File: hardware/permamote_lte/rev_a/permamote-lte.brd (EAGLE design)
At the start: 27 x 60 mm, 116 parts, among them J1 TC2030-JLINK-NL, J2 U.FL-R-SMT, J3 NANO_SIM, J4 U.FL-R-SMT, J5 DM3AT-SF-PEJM5, Q1 PMDXB950UPEL, Q10 PMDXB950UPEL, Q2 PMDXB950UPEL, Q3 PMDXB950UPEL, Q4 PMDXB950UPEL, Q5 PMDXB950UPEL, Q6 PMDXB950UPEL, Q7 PMDXB950UPEL, Q8 PMDXB950UPEL, U1 AB1815-T3, U10 SIP32510, U11 SI7021-A20-GM1, U12 TCS34725, U13 TPD3F303DPVR, U2 BQ25505, U3 EKMB1101111, U4 BGA725L6, U5 NRF9160, U6 LIS2DW12, U7 MAX17222, U8 MAX44009, U9 MS5637-02BA03, X4 ABS07-32.768KHZ-7-T

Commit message: fixes
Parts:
- moved C17 0.77 mm to (21.2, 44.8)
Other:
- board text added: "Permamote_LTE Meghna Mandava 5/20"
- board text removed: "Permamote_LTE Meghna Mandava 4/20"
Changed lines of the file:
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@@
 <?xml version="1.0" encoding="utf-8"?>
 <!DOCTYPE eagle SYSTEM "eagle.dtd">
-<eagle version="9.5.0">
+<eagle version="9.6.1">
 <drawing>
 <settings>
@@
 <text x="0.794" y="27.697" size="1.016" layer="25" font="vector" ratio="12" align="top-left">Permamote_LTE
 Meghna Mandava
-4/20</text>
+5/20</text>
 <polygon width="0.1016" layer="41">
 <vertex x="24.3713" y="17.018"/>
@@
 <wire x1="11.43" y1="37.63" x2="12.6" y2="37.63" width="0.1524" layer="25"/>
 <wire x1="12.6" y1="37.63" x2="12.6" y2="36.106" width="0.1524" layer="25"/>
-<text x="26.416" y="32.639" size="0.8128" layer="25" font="vector" ratio="12" align="center-right">GND</text>
+<text x="26.416" y="32.512" size="0.8128" layer="25" font="vector" ratio="12" align="center-right">GND</text>
 <text x="26.162" y="31.242" size="0.8128" layer="25" font="vector" ratio="12" align="center-right">VCC</text>
 <wire x1="0" y1="60" x2="0.5" y2="60" width="0" layer="20"/>
@@
 <param name="tpViaShape" value="round"/>
 <param name="PrefDir.1" value="-"/>
-<param name="PrefDir.2" value="*"/>
+<param name="PrefDir.2" value="0"/>
 <param name="PrefDir.3" value="0"/>
 <param name="PrefDir.4" value="0"/>
@@
 <param name="PrefDir.13" value="0"/>
 <param name="PrefDir.14" value="0"/>
-<param name="PrefDir.15" value="*"/>
+<param name="PrefDir.15" value="0"/>
 <param name="PrefDir.16" value="|"/>
 <param name="cfVia" value="8"/>
@@
 <attribute name="NAME" x="22.336" y="43.675" size="0.8128" layer="25" font="vector" ratio="12" align="bottom-center"/>
 </element>
-<element name="C17" library="passives" package="0603_CAP" value="10uF" x="21.082" y="45.593" smashed="yes" rot="R180">
-<attribute name="DIGIKEY" value="490-3896-1-ND" x="21.082" y="45.593" size="1.778" layer="27" rot="R180" display="off"/>
-<attribute name="MPN" value="GRM188R60J106ME47D " x="21.082" y="45.593" size="1.778" layer="27" rot="R180" display="off"/>
-<attribute name="NAME" x="19.05" y="45.212" size="0.8128" layer="25" font="vector" ratio="12" align="bottom-center"/>
+<element name="C17" library="passives" package="0603_CAP" value="10uF" x="21.209" y="44.831" smashed="yes" rot="R180">
+<attribute name="DIGIKEY" value="490-3896-1-ND" x="21.209" y="44.831" size="1.778" layer="27" rot="R180" display="off"/>
+<attribute name="MPN" value="GRM188R60J106ME47D " x="21.209" y="44.831" size="1.778" layer="27" rot="R180" display="off"/>
+<attribute name="NAME" x="19.177" y="44.577" size="0.8128" layer="25" font="vector" ratio="12" align="bottom-center"/>
 </element>
 <element name="C18" library="passives" package="0603_CAP" value="10uF" x="18.923" y="40.767" smashed="yes" rot="R180">
@@
 <attribute name="DIGIKEY" value="541-100MAHCT-ND" x="22.352" y="22.352" size="1.778" layer="27" display="off"/>
 <attribute name="MPN" value="HMC0402JT100M " x="22.352" y="22.352" size="1.778" layer="27" display="off"/>
-<attribute name="NAME" x="22.225" y="23.622" size="0.8128" layer="25" font="vector" ratio="12" rot="R180" align="bottom-center"/>
+<attribute name="NAME" x="21.971" y="23.495" size="0.8128" layer="25" font="vector" ratio="12" rot="R180" align="bottom-center"/>
 <attribute name="VALUE" x="22.352" y="20.955" size="1.016" layer="27" font="vector" ratio="12" align="bottom-center"/>
 </element>
@@
 <attribute name="MANUFACTURER" value="NEXPERIA" x="5.334" y="13.843" size="1.778" layer="27" rot="R90" display="off"/>
 <attribute name="MPN" value="PMDXB950UPELZ" x="5.334" y="13.843" size="1.778" layer="27" rot="R90" display="off"/>
-<attribute name="NAME" x="5.334" y="12.954" size="0.8128" layer="25" font="vector" ratio="12" rot="R180" align="bottom-center"/>
+<attribute name="NAME" x="5.334" y="12.446" size="0.8128" layer="25" font="vector" ratio="12" rot="R180" align="bottom-center"/>
 <attribute name="VALUE" x="6.334" y="13.843" size="1.016" layer="27" font="vector" ratio="12" rot="R90" align="top-center"/>
 </element>
@@
 <attribute name="MANUFACTURER" value="NEXPERIA" x="21.082" y="1.905" size="1.778" layer="27" display="off"/>
 <attribute name="MPN" value="PMDXB950UPELZ" x="21.082" y="1.905" size="1.778" layer="27" display="off"/>
-<attribute name="NAME" x="20.955" y="1.159" size="0.8128" layer="25" font="vector" ratio="12" rot="R180" align="bottom-center"/>
+<attribute name="NAME" x="21.082" y="1.032" size="0.8128" layer="25" font="vector" ratio="12" rot="R180" align="bottom-center"/>
 <attribute name="VALUE" x="21.082" y="0.905" size="1.016" layer="27" font="vector" ratio="12" align="top-center"/>
 </element>
@@
 <attribute name="MANUFACTURER" value="NEXPERIA" x="5.334" y="16.383" size="1.778" layer="27" display="off"/>
 <attribute name="MPN" value="PMDXB950UPELZ" x="5.334" y="16.383" size="1.778" layer="27" display="off"/>
-<attribute name="NAME" x="5.334" y="17.272" size="0.8128" layer="25" font="vector" ratio="12" align="bottom-center"/>
+<attribute name="NAME" x="5.334" y="17.526" size="0.8128" layer="25" font="vector" ratio="12" align="bottom-center"/>
 <attribute name="VALUE" x="5.334" y="15.383" size="1.016" layer="27" font="vector" ratio="12" align="top-center"/>
 </element>
@@
 </element>
 <element name="L3" library="passives" package="0402_CAP" value="7.5nH" x="5.842" y="50.927" smashed="yes" rot="R90">
+<attribute name="DIGIKEY" value="490-6565-1-ND" x="5.842" y="50.927" size="1.778" layer="27" rot="R90" display="off"/>
+<attribute name="MPN" value="LQG15HN7N5J02D" x="5.842" y="50.927" size="1.778" layer="27" rot="R90" display="off"/>
 <attribute name="NAME" x="5.461" y="50.927" size="0.8128" layer="25" font="vector" ratio="12" rot="R90" align="bottom-center"/>
 </element>
@@
 </element>
 <element name="L2" library="passives" package="0402_CAP" value="5.1nH" x="5.842" y="52.578" smashed="yes" rot="R90">
+<attribute name="DIGIKEY" value="490-6564-1-ND" x="5.842" y="52.578" size="1.778" layer="27" rot="R90" display="off"/>
+<attribute name="MPN" value="LQG15HN5N1S02D" x="5.842" y="52.578" size="1.778" layer="27" rot="R90" display="off"/>
 <attribute name="NAME" x="6.985" y="52.959" size="0.8128" layer="25" font="vector" ratio="12" rot="R90" align="bottom-center"/>
 </element>
 <element name="L1" library="passives" package="0402_CAP" value="1.8nH" x="7.62" y="51.308" smashed="yes" rot="R180">
+<attribute name="DIGIKEY" value="490-2613-1-ND" x="7.62" y="51.308" size="1.778" layer="27" rot="R180" display="off"/>
+<attribute name="MPN" value="LQG15HS1N8S02D" x="7.62" y="51.308" size="1.778" layer="27" rot="R180" display="off"/>
 <attribute name="NAME" x="7.62" y="52.578" size="0.8128" layer="25" font="vector" ratio="12" rot="R180" align="bottom-center"/>
 </element>
@@
 <attribute name="MANUFACTURER" value="Samsung Electro-Mechanics" x="45.72" y="63.754" size="1.778" layer="27" rot="R270" display="off"/>
 <attribute name="MPN" value="RC1005F103CS" x="45.72" y="63.754" size="1.778" layer="27" rot="R270" display="off"/>
-<attribute name="NAME" x="24.13" y="38.989" size="0.8128" layer="25" font="vector" ratio="12" rot="R270" align="bottom-center"/>
+<attribute name="NAME" x="24.13" y="39.243" size="0.8128" layer="25" font="vector" ratio="12" rot="R270" align="bottom-center"/>
 <attribute name="VALUE" x="22.352" y="38.989" size="1.016" layer="27" font="vector" ratio="12" rot="R270" align="bottom-center"/>
 </element>
@@
 <attribute name="MANUFACTURER" value="Vishay Dale" x="5.715" y="44.704" size="1.778" layer="27" display="off"/>
 <attribute name="MPN" value="CRCW0402100KFKEDHP" x="5.715" y="44.704" size="1.778" layer="27" display="off"/>
-<attribute name="NAME" x="23.749" y="33.02" size="0.8128" layer="25" font="vector" ratio="12" align="bottom-center"/>
+<attribute name="NAME" x="23.876" y="33.02" size="0.8128" layer="25" font="vector" ratio="12" align="bottom-center"/>
 <attribute name="VALUE" x="23.749" y="32.766" size="1.016" layer="27" font="vector" ratio="12" align="bottom-center"/>
 </element>
@@
 <polygon width="0.2032" layer="1" isolate="0.2032" thermals="no">
 <vertex x="21.59" y="42.799"/>
-<vertex x="21.59" y="44.958"/>
-<vertex x="21.209" y="44.958"/>
-<vertex x="21.209" y="46.101"/>
+<vertex x="21.59" y="46.101"/>
 <vertex x="25.527" y="46.101"/>
 <vertex x="25.527" y="43.815"/>
@@
 <wire x1="18.891" y1="44.958" x2="22.86" y2="44.958" width="0.254" layer="16"/>
 <via x="22.86" y="44.958" extent="1-16" drill="0.2032"/>
-<wire x1="21.732" y1="45.593" x2="20.97" y2="44.831" width="0.1524" layer="1"/>
-<wire x1="20.97" y1="44.831" x2="19.035" y2="44.831" width="0.1524" layer="1"/>
-<wire x1="18.273" y1="44.069" x2="19.035" y2="44.831" width="0.1524" layer="1"/>
+<wire x1="21.859" y1="44.831" x2="21.097" y2="45.593" width="0.1524" layer="1"/>
+<wire x1="21.097" y1="45.593" x2="19.797" y2="45.593" width="0.1524" layer="1"/>
+<wire x1="18.273" y1="44.069" x2="19.797" y2="45.593" width="0.1524" layer="1"/>
 </signal>
 <signal name="VBAT">
@@
 <wire x1="14.859" y1="34.036" x2="13.502" y2="34.036" width="0.1524" layer="1"/>
 <wire x1="13.466" y1="34" x2="13.502" y2="34.036" width="0.1524" layer="1"/>
-<via x="12.319" y="13.335" extent="1-16" drill="0.2032"/>
+<via x="12.319" y="13.208" extent="1-16" drill="0.2032"/>
 <via x="18.796" y="36.068" extent="1-16" drill="0.2032"/>
 <wire x1="18.796" y1="36.068" x2="18.796" y2="32.35418125" width="0.4064" layer="1"/>
@@
 <wire x1="14.097" y1="28.575" x2="14.097" y2="22.225" width="0.4064" layer="1"/>
 <wire x1="14.097" y1="22.225" x2="12.319" y2="20.447" width="0.4064" layer="1"/>
-<wire x1="12.319" y1="20.447" x2="12.319" y2="13.335" width="0.4064" layer="1"/>
+<wire x1="12.319" y1="20.447" x2="12.319" y2="13.208" width="0.4064" layer="1"/>
 <wire x1="12.319" y1="4.953" x2="14.097" y2="3.175" width="0.4064" layer="16"/>
-<wire x1="12.319" y1="13.335" x2="12.319" y2="4.953" width="0.4064" layer="16"/>
+<wire x1="12.319" y1="13.208" x2="12.319" y2="4.953" width="0.4064" layer="16"/>
 <wire x1="18.796" y1="32.35418125" x2="18.44581875" y2="32.004" width="0.4064" layer="1"/>
 <wire x1="18.44581875" y1="32.004" x2="18.415" y2="32.004" width="0.4064" layer="1"/>

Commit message: outline, label fixes
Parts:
- moved TP9 3.35 mm to (19.3, 2.16)
- moved R21 0.52 mm to (18.4, 44.2), turned to 90 degrees
- moved U8 0.51 mm to (17.5, 2.54)
- moved Q3 0.38 mm to (17.4, 5.33)
- moved TP1 0.25 mm to (26.0, 5.08)
- moved Q7 0.25 mm to (21.1, 2.16)
- moved C17 0.13 mm to (21.2, 44.7)
- moved R14 0.13 mm to (18.9, 42.3)
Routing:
- net N$14: track 1.85 -> 2.79 mm
- net SDA: track 58.7 -> 57.8 mm
- net !CLR_EN: track 50.5 -> 49.7 mm
- net !LT_INT: track 45.2 -> 44.7 mm
- net GND: track 31.5 -> 31.1 mm, vias 97 -> 99
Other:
- outline, holes or cut-outs redrawn

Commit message: renumber
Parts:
- removed TP30: TEST-POINT, headers:PAD.03X.03
- added TP24: TEST-POINT, headers:PAD.03X.03
- J1: value TC2030-JLINK-NL -> DM3AT-SF-PEJM5; device connector:TC2030-IDC-NL -> connector:DM3AT-SF-PEJM5
- J2: value U.FL-R-SMT -> NANO_SIM; device connector:U.FL_SMT -> signpost:WURTH_NANO_SIM
- J3: value NANO_SIM -> TC2030-JLINK-NL; device signpost:WURTH_NANO_SIM -> connector:TC2030-IDC-NL
- J5: value DM3AT-SF-PEJM5 -> U.FL-R-SMT; device connector:DM3AT-SF-PEJM5 -> connector:U.FL_SMT
- U10: value SIP32510 -> SI7021-A20-GM1; device chips:TSOT23-6 -> chips:DFN-6/3MM
- U11: value SI7021-A20-GM1 -> SIP32510; device chips:DFN-6/3MM -> chips:TSOT23-6
- U2: value BQ25505 -> BGA725L6; device chips:S-PVQFN-N20-RGR -> chips:LNA-TSLP-6-2-ORIG
- U3: value EKMB1101111 -> BQ25505; device chips:AMN2 -> chips:S-PVQFN-N20-RGR
- U4: value BGA725L6 -> EKMB1101111; device chips:LNA-TSLP-6-2-ORIG -> chips:AMN2
- U5: value NRF9160 -> LIS2DW12; device chips:NRF9160 -> chips:LGA-12
- U6: value LIS2DW12 -> MAX17222; device chips:LGA-12 -> chips:UDFN-6-MAXIM
- U7: value MAX17222 -> MAX44009; device chips:UDFN-6-MAXIM -> chips:UDFN-6-EXPOSED
- U8: value MAX44009 -> MS5637-02BA03; device chips:UDFN-6-EXPOSED -> chips:4-SMD
- U9: value MS5637-02BA03 -> NRF9160; device chips:4-SMD -> chips:NRF9160
- moved U3 49.6 mm to (19.9, 53.1), turned to 90 degrees
- moved U4 43.8 mm to (5.50, 5.56), turned to 0 degrees
- moved U7 40.0 mm to (17.5, 2.54)
- moved U10 27.7 mm to (2.02, 19.9)
- moved U11 27.7 mm to (24.1, 36.6)
- moved U6 24.9 mm to (21.7, 42.3), turned to 90 degrees
- moved J2 23.0 mm to (6.99, 35.2), flipped to the bottom, turned to 90 degrees
- moved U9 21.8 mm to (13.7, 31.8)
- moved J3 19.8 mm to (24.5, 26.0), flipped to the top
- moved U8 18.9 mm to (2.03, 13.3)
- moved J5 18.4 mm to (2.29, 51.2), flipped to the top, turned to 90 degrees
- moved J1 18.3 mm to (18.9, 43.4), flipped to the bottom, turned to 180 degrees
- moved U5 17.8 mm to (24.4, 17.5), turned to 0 degrees
- moved U2 14.8 mm to (5.59, 49.4)
- moved TP25 10.3 mm to (25.4, 30.5)
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- renumbered BAT1 to BT2, Q10 to Q9, TP31 to TP28, TP32 to TP29, X4 to X1
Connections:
- net !CLR_EN: now also U9.P0.08; no longer U5.P0.08
- net !CLR_INT: now also U9.P0.29; no longer U5.P0.29
- net !HUM_EN: now also U9.P0.04; no longer U5.P0.04
- net !LT_EN: now also U9.P0.30; no longer U5.P0.30
- net !LT_INT: now also U7.4, U9.P0.02; no longer U5.P0.02, U8.4
- net !PIR_EN: now also U9.P0.24; no longer U5.P0.24
- net !PR_EN: now also U9.P0.23; no longer U5.P0.23
- net !RST: now also J3.3, U9.NRESET; no longer J1.3, U5.NRESET
- net !RTC_IRQ1: now also U9.P0.11; no longer U5.P0.11
- net !RTC_IRQ2: now also U9.P0.10; no longer U5.P0.10
- net !RTC_IRQ3: now also U9.P0.09; no longer U5.P0.09
- net !SD_CS: now also J1.2, U9.P0.26; no longer J5.2, U5.P0.26
- net !SD_DETECT: now also J1.A, U9.P0.27; no longer J5.A, U5.P0.27
- net !VBAT_PRI_ON: now also U3.10; no longer U2.10
- net !VBAT_SEC_ON: now also U3.9; no longer U2.9
- net ACC_CS: now also U5.2, U9.P0.06; no longer U5.P0.06, U6.2
- net ACC_INT1: now also U5.12, U9.P0.05; no longer U5.P0.05, U6.12
- net ACC_INT2: now also U5.11, U9.P0.07; no longer U5.P0.07, U6.11
- net GND: now also J1.6, J1.B, J1.MOUNT0, J1.MOUNT1, J1.MOUNT2, J1.MOUNT3, J2.C5, J3.5, J5.GND1, J5.GND2, TP26.P$1, U10.2, U11.4, U2.4, U3.1, U3.15, U3.16, U3.17, U3.5, U3.6, U3.PAD, U4.GND, U5.5, U5.6, U5.7, U5.8, U6.3, U7.2, U7.EP, U8.4, U9.GND@1, U9.GND@10, U9.GND@11, U9.GND@12, U9.GND@13, U9.GND@14, U9.GND@15, U9.GND@16, U9.GND@17, U9.GND@18, U9.GND@19, U9.GND@2, U9.GND@20, U9.GND@21, U9.GND@22, U9.GND@23, U9.GND@24, U9.GND@25, U9.GND@26, U9.GND@27, U9.GND@28, U9.GND@29, U9.GND@3, U9.GND@30, U9.GND@31, U9.GND@32, U9.GND@33, U9.GND@34, U9.GND@35, U9.GND@4, U9.GND@5, U9.GND@6, U9.GND@7, U9.GND@8, U9.GND@9, U9.GND_SHIELD@1, U9.GND_SHIELD@10, U9.GND_SHIELD@11, U9.GND_SHIELD@12, U9.GND_SHIELD@13, U9.GND_SHIELD@14, U9.GND_SHIELD@15, U9.GND_SHIELD@16, U9.GND_SHIELD@17, U9.GND_SHIELD@18, U9.GND_SHIELD@19, U9.GND_SHIELD@2, U9.GND_SHIELD@20, U9.GND_SHIELD@21, U9.GND_SHIELD@22, U9.GND_SHIELD@23, U9.GND_SHIELD@24, U9.GND_SHIELD@25, U9.GND_SHIELD@26, U9.GND_SHIELD@27, U9.GND_SHIELD@28, U9.GND_SHIELD@29, U9.GND_SHIELD@3, U9.GND_SHIELD@30, U9.GND_SHIELD@31, U9.GND_SHIELD@32, U9.GND_SHIELD@33, U9.GND_SHIELD@34, U9.GND_SHIELD@4, U9.GND_SHIELD@5, U9.GND_SHIELD@6, U9.GND_SHIELD@7, U9.GND_SHIELD@8, U9.GND_SHIELD@9; no longer J1.5, J2.GND1, J2.GND2, J3.C5, J5.6, J5.B, J5.MOUNT0, J5.MOUNT1, J5.MOUNT2, J5.MOUNT3, TP27.P$1, U10.4, U11.2, U2.15, U2.16, U2.17, U2.5, U2.6, U2.PAD, U3.GND, U4.1, U4.4, U5.GND@1, U5.GND@10, U5.GND@11, U5.GND@12, U5.GND@13, U5.GND@14, U5.GND@15, U5.GND@16, U5.GND@17, U5.GND@18, U5.GND@19, U5.GND@2, U5.GND@20, U5.GND@21, U5.GND@22, U5.GND@23, U5.GND@24, U5.GND@25, U5.GND@26, U5.GND@27, U5.GND@28, U5.GND@29, U5.GND@3, U5.GND@30, U5.GND@31, U5.GND@32, U5.GND@33, U5.GND@34, U5.GND@35, U5.GND@4, U5.GND@5, U5.GND@6, U5.GND@7, U5.GND@8, U5.GND@9, U5.GND_SHIELD@1, U5.GND_SHIELD@10, U5.GND_SHIELD@11, U5.GND_SHIELD@12, U5.GND_SHIELD@13, U5.GND_SHIELD@14, U5.GND_SHIELD@15, U5.GND_SHIELD@16, U5.GND_SHIELD@17, U5.GND_SHIELD@18, U5.GND_SHIELD@19, U5.GND_SHIELD@2, U5.GND_SHIELD@20, U5.GND_SHIELD@21, U5.GND_SHIELD@22, U5.GND_SHIELD@23, U5.GND_SHIELD@24, U5.GND_SHIELD@25, U5.GND_SHIELD@26, U5.GND_SHIELD@27, U5.GND_SHIELD@28, U5.GND_SHIELD@29, U5.GND_SHIELD@3, U5.GND_SHIELD@30, U5.GND_SHIELD@31, U5.GND_SHIELD@32, U5.GND_SHIELD@33, U5.GND_SHIELD@34, U5.GND_SHIELD@4, U5.GND_SHIELD@5, U5.GND_SHIELD@6, U5.GND_SHIELD@7, U5.GND_SHIELD@8, U5.GND_SHIELD@9, U6.5, U6.6, U6.7, U6.8, U8.2, U8.3, U8.EP, U9.4
- net GPS_EN: now also U2.6, U9.MAGPIO0; no longer U4.6, U5.MAGPIO0
- net LBST: now also U3.20; no longer U2.20
- net LED_BLUE: now also U9.P0.17; no longer U5.P0.17
- net LED_GREEN: now also U9.P0.19; no longer U5.P0.19
- net LED_RED: now also U9.P0.18; no longer U5.P0.18
- net MISO: now also J1.7, U5.3, U9.P0.22; no longer J5.7, U5.P0.22, U6.3
- net MOSI: now also J1.3, U5.4, U9.P0.21; no longer J5.3, U5.P0.21, U6.4
- net N$1: now also U2.3, U9.GPS; no longer U4.3, U5.GPS
- net N$12: now also U6.4; no longer U7.4
- net N$13: now also J1.4, U11.1, U11.2; no longer J5.4, U10.1, U10.2
- net N$14: now also U6.6; no longer U7.6
- net N$18: now also U3.7; no longer U2.7
- net N$2: now also U2.5; no longer U4.5
- net N$20: now also U7.1; no longer U8.1
- net N$21: now also U8.1; no longer U9.1
- net N$22: now also U10.5; no longer U11.5
- net N$23: now also U4.VCC; no longer U3.VCC
- net N$28: now also U9.ENABLE; no longer U5.ENABLE
- net N$29: now also U9.IO_SUPPLY; no longer U5.IO_SUPPLY
- net N$32: now also U3.8; no longer U2.8
- net N$34: now also U8.3; no longer U9.3
- net N$4: now also J5.SIG; no longer J4.SIG
- net N$41: now also U8.2; no longer U9.2
- net N$48: now also U10.1; no longer U11.1
- net N$50: now also U10.6; no longer U11.6
- net N$51: now also U7.6; no longer U8.6
- net N$52: now also U7.5; no longer U8.5
- net N$57: now also U3.12; no longer U2.12
- net N$58: now also U3.11; no longer U2.11
- net N$8: now also J4.SIG, U9.ANT; no longer J2.SIG, U5.ANT
- net PIR_OUT: now also U4.OUT, U9.P0.25; no longer U3.OUT, U5.P0.25
- net RTC_CS: now also U9.P0.12; no longer U5.P0.12
- net SCK: now also J1.5, U5.1, U9.P0.03; no longer J5.5, U5.P0.03, U6.1
- net SCL: now also U9.P0.01; no longer U5.P0.01
- net SDA: now also U9.P0.00; no longer U5.P0.00
- net SD_ENABLE: now also U11.3, U9.P0.28; no longer U10.3, U5.P0.28
- net SIM_1V8: now also J2.C1, U9.SIM_1V8; no longer J3.C1, U5.SIM_1V8
- net SIM_CLK: now also U9.SIM_CLK; no longer U5.SIM_CLK
- net SIM_CLK2: now also J2.C3; no longer J3.C3
- net SIM_IO: now also U9.SIM_IO; no longer U5.SIM_IO
- net SIM_IO2: now also J2.C7; no longer J3.C7
- net SIM_RST: now also U9.SIM_RST; no longer U5.SIM_RST
- net SIM_RST2: now also J2.C2, TP27.P$1; no longer J3.C2, TP30.P$1
- net SW: now also TP24.P$1, U6.2; no longer TP25.P$1, U7.2
- net SWDCLK: now also J3.4, U9.SWDCLK; no longer J1.4, U5.SWDCLK
- net SWDIO: now also J3.2, U9.SWDIO; no longer J1.2, U5.SWDIO
- net VBAT: now also U3.14, U9.P0.15; no longer U2.14, U5.P0.15
- net VBAT_OK: now also U3.13, U9.P0.20; no longer U2.13, U5.P0.20
- net VCC: now also J3.1, TP25.P$1, U11.5, U11.6, U2.2, U5.10, U5.9, U6.1, U9.VDD@1, U9.VDD@2, U9.VDD_GPIO; no longer J1.1, TP26.P$1, U10.5, U10.6, U4.2, U5.VDD@1, U5.VDD@2, U5.VDD_GPIO, U6.10, U6.9, U7.1
- net VOC_SAMP_VSTOR: now also U3.19, U3.3; no longer U2.19, U2.3
- net VREF_SAMP: now also U3.4; no longer U2.4
- net VSEC: now also U3.18, U9.P0.13; no longer U2.18, U5.P0.13
- net VSOL: now also U3.2, U9.P0.14; no longer U2.2, U5.P0.14
- net VSW: now also U6.5; no longer U7.5
- net WDI: now also U9.P0.16; no longer U5.P0.16

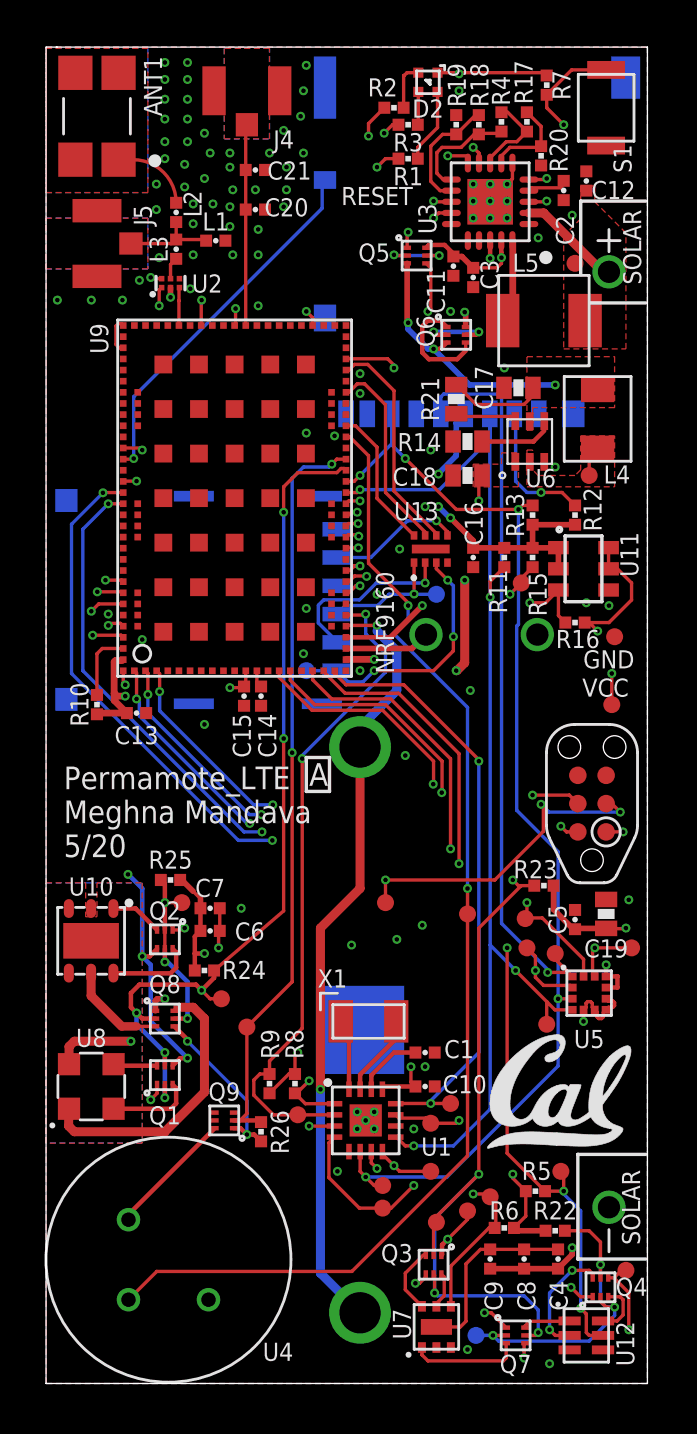
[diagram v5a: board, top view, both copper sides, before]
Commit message: pins overlapping cage need to fix
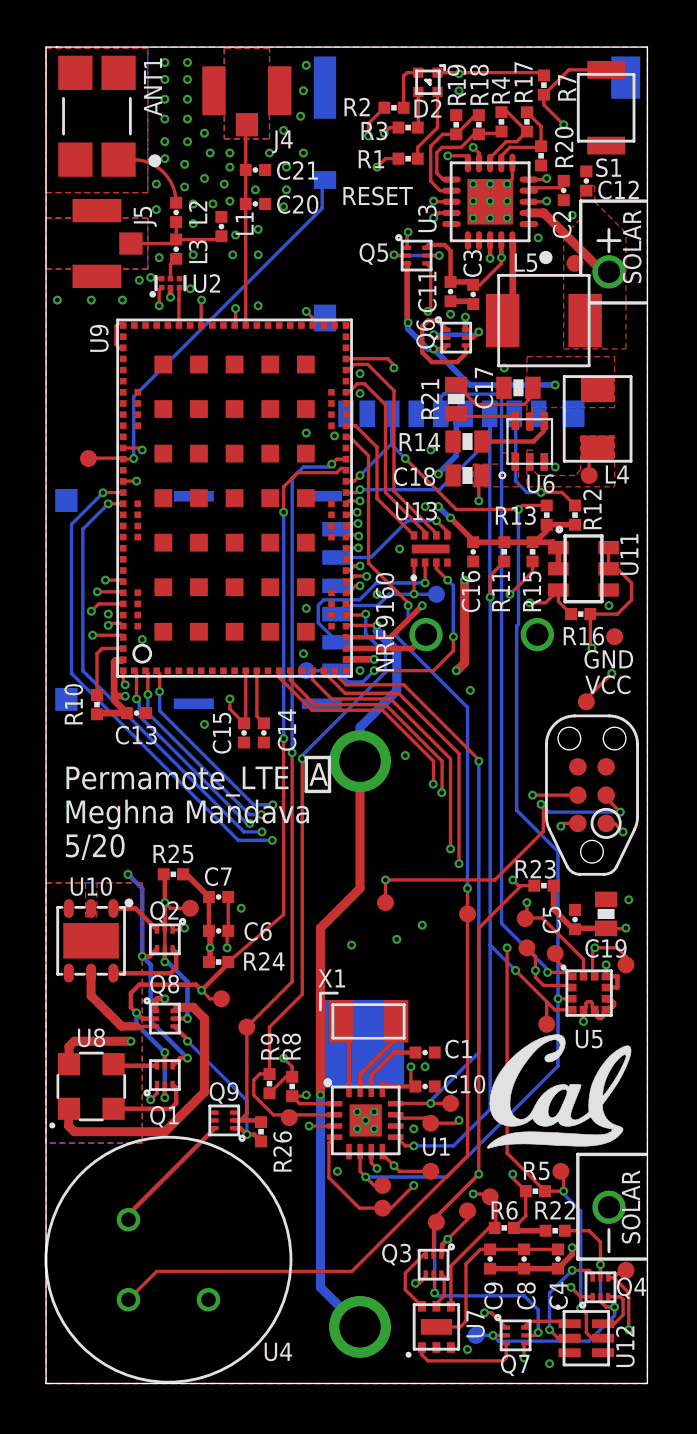
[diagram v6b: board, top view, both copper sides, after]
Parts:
- moved TP29 20.2 mm to (1.91, 41.5)
- moved C14 1.66 mm to (9.78, 29.2)
- moved C15 1.65 mm to (8.89, 29.2)
- moved C11 1.15 mm to (18.2, 49.0)
- moved TP25 1.15 mm to (24.3, 30.6)
- moved TP19 0.80 mm to (26.0, 18.8)
- moved C3 0.76 mm to (19.2, 48.9)
- moved R24 0.74 mm to (7.75, 18.9)
- moved L1 0.68 mm to (7.87, 51.9), turned to 270 degrees
- moved C7 0.64 mm to (7.75, 21.8)
- moved BT2 0.63 mm to (14.1, 15.2)
- moved R13 0.63 mm to (22.5, 39.0)
- moved R16 0.46 mm to (24.0, 34.5)
- moved TP12 0.46 mm to (6.48, 21.3)
- moved TP16 0.40 mm to (10.9, 11.9)
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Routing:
- net VCC: track 62.9 -> 65.4 mm
- net !SD_DETECT: track 40.2 -> 42.1 mm
- net GND: track 31.1 -> 32.8 mm, vias 99 -> 98
- net N$29: track 0.78 -> 2.49 mm
- net VOC_SAMP_VSTOR: track 9.24 -> 10.6 mm
- net !RST: track 45.0 -> 45.8 mm
- net VBAT: track 63.2 -> 64.0 mm
- net N$4: track 4.29 -> 4.98 mm
- net !HUM_EN: track 23.6 -> 24.2 mm
- net MISO: track 52.4 -> 53.1 mm
- net N$13: track 14.9 -> 14.4 mm
